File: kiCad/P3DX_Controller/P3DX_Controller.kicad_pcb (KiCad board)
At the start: 2 copper layers, 125 x 80 mm, 25 parts, among them J1 Conn_01x10_Pin, J2 Conn_01x26_Pin, J3 Conn_01x10_Pin, J4 Conn_01x16_Pin, J5 Conn_01x03_Pin, J6 Conn_01x05_Pin, U1 TXS0108EPW, U3 ESP32-DevKitC

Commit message: 20251201
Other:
- board text added: "Pioneer 3DX Mobile Robot Controller Department: ATIx/Mechatronics Design by: Gerard Harkema © 2025 https://avansmechatronica.github.io/pioneer3dx_ROS2/"
- board text removed: "Pioneer 3DX Mobile Robot Controller Department: ATIx/Mechatronics Design by: Gerard Harkema © 2025"
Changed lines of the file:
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@@
 		)
 	)
-	(gr_text "Pioneer 3DX Mobile Robot Controller\nDepartment: ATIx/Mechatronics\nDesign by: Gerard Harkema © 2025\n"
+	(gr_text "Pioneer 3DX Mobile Robot Controller\nDepartment: ATIx/Mechatronics\nDesign by: Gerard Harkema © 2025\nhttps://avansmechatronica.github.io/pioneer3dx_ROS2/"
 		(locked yes)
 		(at 111.95 125.6 0)

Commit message: 20251202
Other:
- board text added: "User Control Panel"
- board text removed: "User Panel Control"
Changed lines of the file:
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@@
 			(outputformat 1)
 			(mirror no)
-			(drillshape 1)
+			(drillshape 0)
 			(scaleselection 1)
-			(outputdirectory "")
+			(outputdirectory "Gerber/")
 		)
 	)
@@
 		)
 	)
-	(gr_text "User Panel Control"
+	(gr_text "User Control Panel"
 		(at 51.9225 88.9233 90)
 		(layer "F.SilkS")
@@
 				)
 			)
+		)
+	)
+	(dimension
+		(type orthogonal)
+		(layer "User.2")
+		(pts
+			(xy 175 130) (xy 175 50)
+		)
+		(height 23.5)
+		(orientation 1)
+		(format
+			(prefix "")
+			(suffix "")
+			(units 2)
+			(units_format 0)
+			(precision 1)
+		)
+		(style
+			(thickness 0.1)
+			(arrow_length 1.27)
+			(text_position_mode 0)
+			(arrow_direction outward)
+			(extension_height 0.58642)
+			(extension_offset 0.5)
+			(keep_text_aligned yes)
+		)
+		(gr_text "80,0"
+			(at 197.35 90 90)
+			(layer "User.2")
+			(effects
+				(font
+					(size 1 1)
+					(thickness 0.15)
+				)
+			)
+		)
+	)
+	(dimension
+		(type orthogonal)
+		(layer "User.2")
+		(pts
+			(xy 50 130) (xy 175 130)
+		)
+		(height 10.5)
+		(orientation 0)
+		(format
+			(prefix "")
+			(suffix "")
+			(units 2)
+			(units_format 1)
+			(precision 4)
+		)
+		(style
+			(thickness 0.1)
+			(arrow_length 1.27)
+			(text_position_mode 0)
+			(arrow_direction outward)
+			(extension_height 0.58642)
+			(extension_offset 0.5)
+			(keep_text_aligned yes)
+		)
+		(gr_text "125,0000 mm"
+			(at 112.5 139.35 0)
+			(layer "User.2")
+			(effects
+				(font
+					(size 1 1)
+					(thickness 0.15)
+				)
+			)

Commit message: 20251202
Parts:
- removed the R5 at (146.2, 63.5)
- removed U4: ~, p3dx:MPU6050
- added J6: Conn_01x03_Pin, Connector_PinHeader_2.54mm:PinHeader_1x03_P2.54mm_Vertical, F.Cu at (129.1, 70.9)
- added R4: DO NOT PLACE, Resistor_THT:R_Axial_DIN0204_L3.6mm_D1.6mm_P7.62mm_Horizontal, F.Cu at (64.7, 71.8)
- moved R5 10.7 mm to (64.7, 77.9), turned to -90 degrees
- moved U1 9.10 mm to (87.4, 82.4)
- moved CP1 4.10 mm to (119.3, 79.1)
- moved CP2 4.10 mm to (119.3, 69.8)
- moved C1 4.10 mm to (116.8, 74.5)
- moved C2 4.10 mm to (116.8, 83.8)
- renumbered C3 to C1, C4 to C2, G*** to G1, HOLE4 to HOLE3, HOLE3 to HOLE4, J6 to J7, R4 to R1, R1 to R2, R2 to R5, U3 to U2, U2 to U3
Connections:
- J1 pad 1: /front_bumper -> /bumper
- J1 pad 2: /front_bumper -> /bumper
- J1 pad 3: /front_bumper -> /bumper
- J1 pad 4: /front_bumper -> /bumper
- J1 pad 5: /front_bumper -> /bumper
- J1 pad 6: /front_bumper -> /bumper
- J1 pad 7: /front_bumper -> /bumper
- J1 pad 8: /front_bumper -> /bumper
- J3 pad 1: /rear_bumper -> /bumper
- J3 pad 2: /rear_bumper -> /bumper
- J3 pad 3: /rear_bumper -> /bumper
- J3 pad 4: /rear_bumper -> /bumper
- J3 pad 5: /rear_bumper -> /bumper
- J3 pad 6: /rear_bumper -> /bumper
- J3 pad 7: /rear_bumper -> /bumper
- J3 pad 8: /rear_bumper -> /bumper
- R1 pad 2: /front_bumper -> /bumper
- U2 pad 12: /imu_int -> /lidar-motor
- U2 pad 16: /R_ENCODER_A_LV -> unconnected-(U3-SD_DATA2/GPIO9-Pad16)
- U2 pad 17: /L_ENCODER_A_LV -> unconnected-(U3-SD_DATA3/GPIO10-Pad17)
- U2 pad 20: /R_MOTOR_DIR -> unconnected-(U3-SD_CLK/GPIO6-Pad20)
- U2 pad 21: /L_ENCODER_B_LV -> unconnected-(U3-SD_DATA0/GPIO7-Pad21)
- U2 pad 22: /R_ENCODER_B_LV -> unconnected-(U3-SD_DATA1/GPIO8-Pad22)
- U2 pad 24: unconnected-(U3-ADC2_CH2/GPIO2-Pad24) -> /R_ENCODER_B_LV
- U2 pad 25: unconnected-(U3-GPIO0/BOOT/ADC2_CH1-Pad25) -> /L_ENCODER_B_LV
- U2 pad 33: /i2c-sda -> /R_ENCODER_A_LV
- U2 pad 36: /i2c-scl -> /L_ENCODER_A_LV
- U2 pad 7: /front_bumper -> /R_MOTOR_DIR
- U2 pad 8: /rear_bumper -> /bumper
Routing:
- net /bumper: track 0.00 -> 150.0 mm
- net /rear_bumper: track 123.5 -> 0.00 mm, vias 1 -> 0
- net /lidar-motor: track 0.00 -> 80.1 mm
- net /front_bumper: track 55.5 -> 0.00 mm
- net +3V3: track 170.2 -> 117.1 mm, vias 1 -> 0
- net /R_MOTOR_DIR: track 129.7 -> 77.8 mm
- net /i2c-scl: track 47.2 -> 0.00 mm, vias 1 -> 0
- net /i2c-sda: track 41.5 -> 0.00 mm
- net /imu_int: track 22.7 -> 0.00 mm, vias 1 -> 0
- net /ucp_status_lv: track 95.4 -> 75.3 mm, vias 2 -> 1
- net /L_ENCODER_B_LV: track 81.0 -> 61.5 mm
- net /ucp_motors_lv: track 28.8 -> 13.2 mm, vias 1 -> 0
- net /L_ENCODER_B: track 20.0 -> 35.4 mm, vias 0 -> 1
- net /R_ENCODER_B_LV: track 77.2 -> 62.4 mm
- net /ucp_motors: track 72.0 -> 58.5 mm
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
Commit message: 20251203
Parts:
- added R6: DO NOT PLACE, Resistor_THT:R_Axial_DIN0204_L3.6mm_D1.6mm_P7.62mm_Horizontal, F.Cu at (137.0, 137.1)
- U2: value ESP32-DevKitC -> ESP32-S3-DevKitC; footprint PCM_Espressif:ESP32-DevKitC -> PCM_Espressif:ESP32-S3-DevKitC
- moved U2 14.6 mm to (112.9, 94.1)
- turned U3 to 180 degrees
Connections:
- U2 pad 10: /L_MOTOR_DIR -> unconnected-(U2-GPIO17/ADC2_CH6-Pad10)
- U2 pad 11: /R_MOTOR_PWM -> unconnected-(U2-GPIO18/ADC2_CH7-Pad11)
- U2 pad 12: /lidar-motor -> unconnected-(U2-GPIO8/ADC1_CH7-Pad12)
- U2 pad 13: /display_RS_DC -> unconnected-(U2-GPIO3/ADC1_CH2-Pad13)
- U2 pad 14: GND -> unconnected-(U2-GPIO46-Pad14)
- U2 pad 15: /display_rst -> unconnected-(U2-GPIO9/ADC1_CH8-Pad15)
- U2 pad 19: VCC -> unconnected-(U2-GPIO13/ADC2_CH2-Pad19)
- U2 pad 2: unconnected-(U3-CHIP_PU-Pad2) -> +3V3
- U2 pad 21: unconnected-(U3-SD_DATA0/GPIO7-Pad21) -> VCC
- U2 pad 22: unconnected-(U3-SD_DATA1/GPIO8-Pad22) -> GND
- U2 pad 23: /ucp_status_lv -> GND
- U2 pad 24: /R_ENCODER_B_LV -> GND
- U2 pad 25: /L_ENCODER_B_LV -> unconnected-(U2-GPIO19/USB_D--Pad25)
- U2 pad 26: /MOTOR_ENABLE -> unconnected-(U2-GPIO20/USB_D+-Pad26)
- U2 pad 27: /lidar-tx -> unconnected-(U2-GPIO21-Pad27)
- U2 pad 28: /lidar-rx -> unconnected-(U2-GPIO47-Pad28)
- U2 pad 29: /display_cs -> unconnected-(U2-GPIO48-Pad29)
- U2 pad 3: /ucp_motors_lv -> unconnected-(U2-CHIP_PU-Pad3)
- U2 pad 30: /display_clk -> unconnected-(U2-GPIO45-Pad30)
- U2 pad 31: /display_not_used -> unconnected-(U2-GPIO0-Pad31)
- U2 pad 32: GND -> unconnected-(U2-GPIO35-Pad32)
- U2 pad 33: /R_ENCODER_A_LV -> unconnected-(U2-GPIO36-Pad33)
- U2 pad 36: /L_ENCODER_A_LV -> unconnected-(U2-GPIO39/MTCK-Pad36)
- U2 pad 37: /display_sda -> unconnected-(U2-GPIO40/MTDO-Pad37)
- U2 pad 38: GND -> unconnected-(U2-GPIO41/MTDI-Pad38)
- U2 pad 4: /ucp_buzzer_pwm_lv -> unconnected-(U2-GPIO4/ADC1_CH3-Pad4)
- U2 pad 5: /V_BATTERY_MEASUREMENT -> unconnected-(U2-GPIO5/ADC1_CH4-Pad5)
- U2 pad 6: /ucp_reset_lv -> unconnected-(U2-GPIO6/ADC1_CH5-Pad6)
- U2 pad 7: /R_MOTOR_DIR -> unconnected-(U2-GPIO7/ADC1_CH6-Pad7)
- U2 pad 8: /bumper -> unconnected-(U2-GPIO15/ADC2_CH4/32K_P-Pad8)
- U2 pad 9: /L_MOTOR_PWM -> unconnected-(U2-GPIO16/ADC2_CH5/32K_N-Pad9)
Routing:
- net /bumper: track 150.0 -> 0.00 mm
- net VCC: track 149.6 -> 0.00 mm
- net +3V3: track 117.1 -> 0.00 mm
- net /lidar-tx: track 115.4 -> 0.00 mm, vias 1 -> 0
- net /MOTOR_ENABLE: track 113.7 -> 0.00 mm, vias 1 -> 0
- net /lidar-rx: track 111.5 -> 0.00 mm, vias 1 -> 0
- net /L_MOTOR_PWM: track 86.1 -> 0.00 mm, vias 2 -> 0
- net /L_MOTOR_DIR: track 85.7 -> 0.00 mm, vias 1 -> 0
- net /R_MOTOR_PWM: track 82.4 -> 0.00 mm, vias 1 -> 0
- net /lidar-motor: track 80.1 -> 0.00 mm
- net /R_MOTOR_DIR: track 77.8 -> 0.00 mm, vias 1 -> 0
- net /ucp_status_lv: track 75.3 -> 0.00 mm, vias 1 -> 0
- net /R_ENCODER_B_LV: track 62.4 -> 0.00 mm, vias 1 -> 0
- net /L_ENCODER_B_LV: track 61.5 -> 0.00 mm, vias 1 -> 0
- net /ucp_motors: track 58.5 -> 0.00 mm, vias 1 -> 0
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
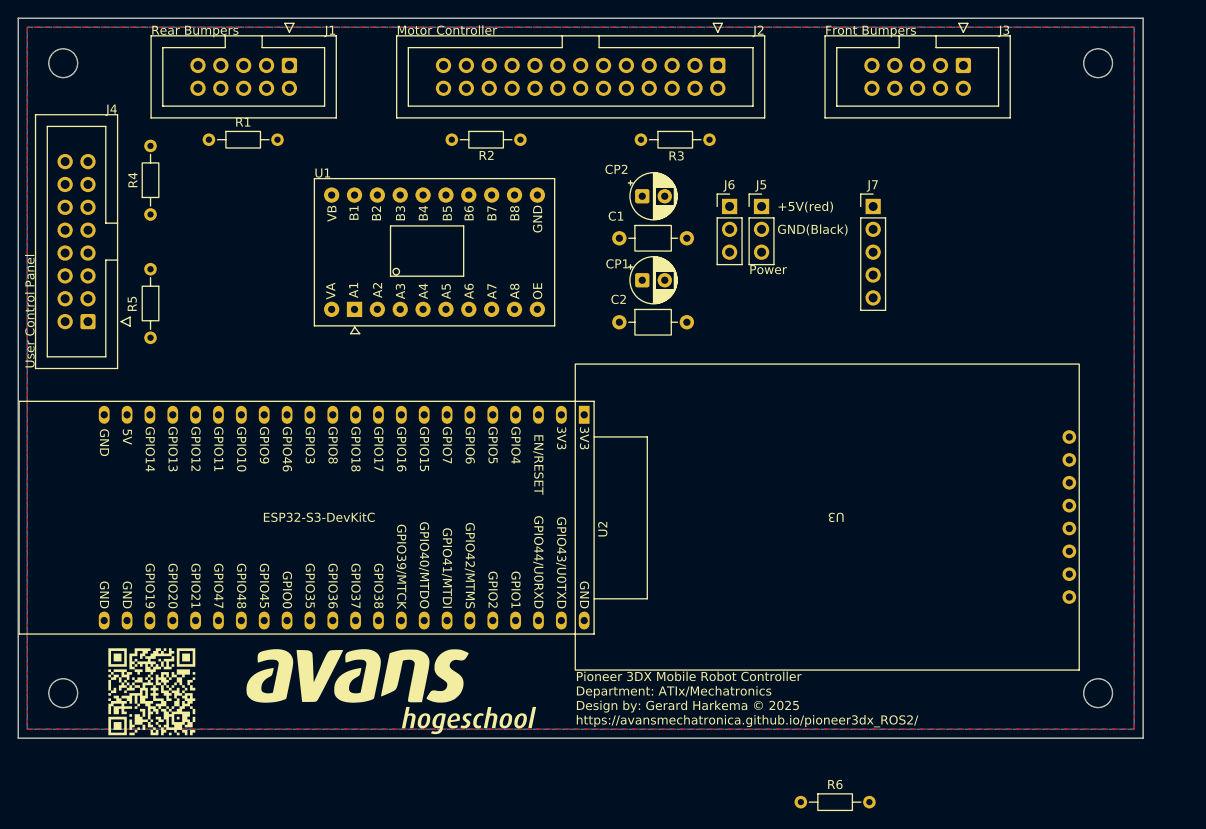
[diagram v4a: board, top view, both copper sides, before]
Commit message: esp32-s3 change
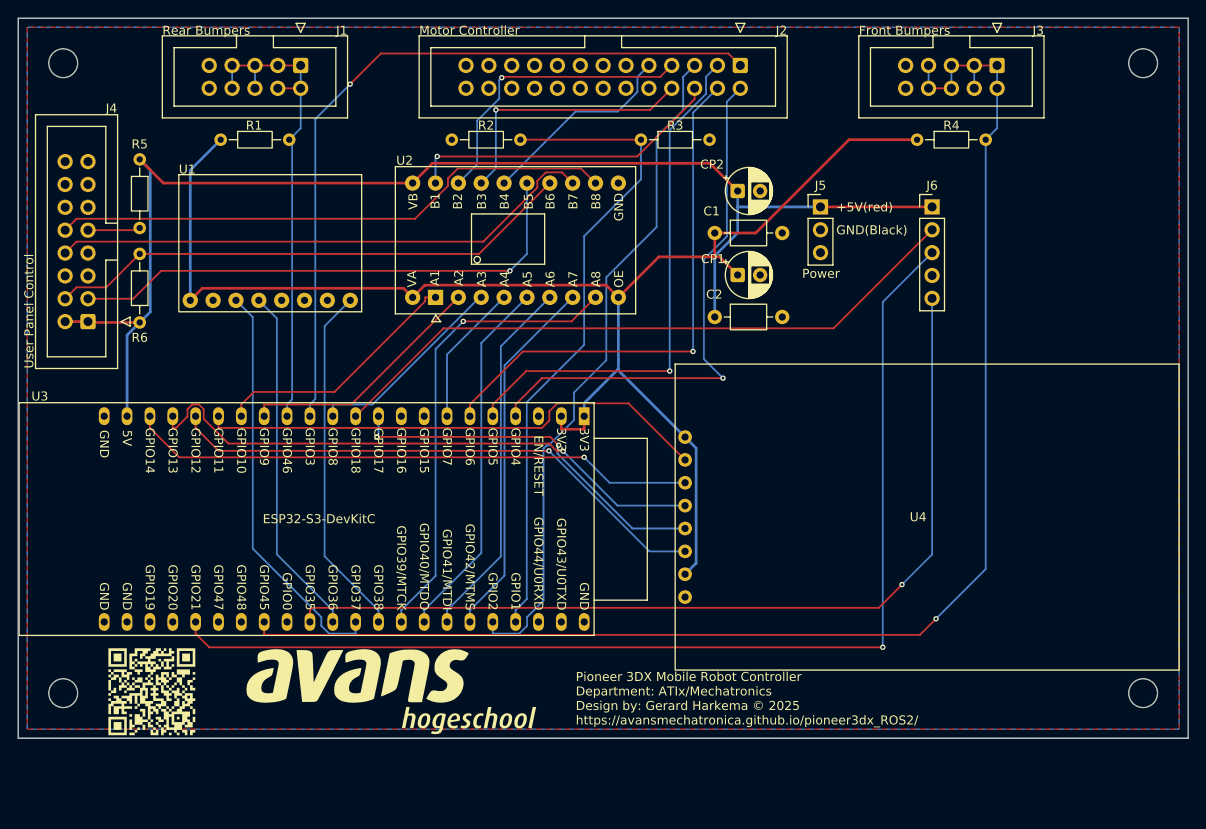
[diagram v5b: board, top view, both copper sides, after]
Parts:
- removed the J6 at (129.1, 70.9)
- removed the R6 at (137.0, 137.1)
- removed the U2 at (112.9, 94.1)
- added R5: DO NOT PLACE, Resistor_THT:R_Axial_DIN0204_L3.6mm_D1.6mm_P7.62mm_Horizontal, F.Cu at (63.5, 65.7)
- added U1: ~, p3dx:MPU6050, F.Cu at (64.0, 76.3)
- added U3: ESP32-S3-DevKitC, PCM_Espressif:ESP32-S3-DevKitC, F.Cu at (112.9, 94.2)
- moved R4 85.6 mm to (149.9, 63.5), turned to 0 degrees
- moved U4 11.1 mm to (151.0, 105.4), turned to 0 degrees
- moved C1 10.6 mm to (127.4, 73.9)
- moved C2 10.6 mm to (127.4, 83.2)
- moved CP1 10.6 mm to (129.9, 78.5)
- moved CP2 10.6 mm to (129.9, 69.2)
- moved U2 9.10 mm to (96.4, 81.0)
- moved J5 6.55 mm to (139.2, 71.0)
- moved J6 6.55 mm to (151.6, 71.0)
- moved R6 6.04 mm to (63.5, 83.8), turned to 90 degrees
- moved HOLE2 5.00 mm to (175.0, 55.0)
- moved HOLE4 5.00 mm to (175.0, 125.0)
- moved J3 3.75 mm to (158.8, 55.2)
- moved J2 2.50 mm to (130.2, 55.2)
- moved R1 1.31 mm to (72.5, 63.5)
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- renumbered G*** to G2, J7 to J6, R5 to R6, U1 to U2, U3 to U4
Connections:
- J1 pad 1: /bumper -> /front_bumper
- J1 pad 2: /bumper -> /front_bumper
- J1 pad 3: /bumper -> /front_bumper
- J1 pad 4: /bumper -> /front_bumper
- J1 pad 5: /bumper -> /front_bumper
- J1 pad 6: /bumper -> /front_bumper
- J1 pad 7: /bumper -> /front_bumper
- J1 pad 8: /bumper -> /front_bumper
- J3 pad 1: /bumper -> /rear_bumper
- J3 pad 2: /bumper -> /rear_bumper
- J3 pad 3: /bumper -> /rear_bumper
- J3 pad 4: /bumper -> /rear_bumper
- J3 pad 5: /bumper -> /rear_bumper
- J3 pad 6: /bumper -> /rear_bumper
- J3 pad 7: /bumper -> /rear_bumper
- J3 pad 8: /bumper -> /rear_bumper
- R1 pad 2: /bumper -> /front_bumper
- R4 pad 1: VCC -> +3V3
- R4 pad 2: /ucp_power_led -> /rear_bumper
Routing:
- net +3V3: track 0.00 -> 161.4 mm
- net /rear_bumper: track 0.00 -> 156.3 mm, vias 0 -> 1
- net VCC: track 0.00 -> 144.8 mm
- net /lidar-rx: track 0.00 -> 124.4 mm, vias 0 -> 1
- net /lidar-motor: track 0.00 -> 101.5 mm, vias 0 -> 1
- net /L_MOTOR_PWM: track 0.00 -> 84.1 mm, vias 0 -> 1
- net /MOTOR_ENABLE: track 0.00 -> 75.6 mm
- net /V_BATTERY_MEASUREMENT: track 0.00 -> 72.7 mm
- net /lidar-tx: track 0.00 -> 72.6 mm
- net /display_rst: track 0.00 -> 65.1 mm, vias 0 -> 1
- net /display_RS_DC: track 0.00 -> 63.3 mm, vias 0 -> 1
- net /ucp_status: track 0.00 -> 62.9 mm
- net /display_clk: track 0.00 -> 61.4 mm, vias 0 -> 1
- net /ucp_buzzer_pwm: track 0.00 -> 61.0 mm
- net /L_MOTOR_DIR: track 0.00 -> 60.3 mm, vias 0 -> 1
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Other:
- board size 125 x 80 mm -> 130 x 80 mm
- board text added: "User Panel Control"
- board text removed: "User Control Panel"

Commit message: 20251204
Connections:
- J2 pad 10: unconnected-(J2-Pin_10-Pad10) -> /R_ENCODER_B
- J2 pad 12: unconnected-(J2-Pin_12-Pad12) -> /L_ENCODER_B
- J2 pad 22: GND -> /V_BATTERY
- J2 pad 7: /R_ENCODER_A -> unconnected-(J2-Pin_7-Pad7)
- J2 pad 8: /R_ENCODER_B -> /R_ENCODER_A
- J2 pad 9: /L_ENCODER_B -> unconnected-(J2-Pin_9-Pad9)
- J4 pad 11: unconnected-(J4-Pin_11-Pad11) -> /V_BATTERY
- J4 pad 12: GND -> unconnected-(J4-Pin_12-Pad12)
- R2 pad 1: GND -> /V_BATTERY
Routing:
- net /V_BATTERY: track 0.00 -> 53.9 mm
- net /R_MOTOR_DIR: track 58.9 -> 87.5 mm
- net /display_clk: track 61.4 -> 80.7 mm, vias 1 -> 2
- net VCC: track 144.8 -> 155.8 mm, vias 0 -> 1
- net /display_cs: track 57.5 -> 68.2 mm, vias 0 -> 3
- net /lidar-tx: track 72.6 -> 83.0 mm, vias 0 -> 1
- net /display_rst: track 65.1 -> 74.0 mm, vias 1 -> 2
- net /display_sda: track 41.6 -> 50.2 mm, vias 2 -> 1
- net /display_RS_DC: track 63.3 -> 71.4 mm, vias 1 -> 0
- net +3V3: track 161.4 -> 167.5 mm, vias 0 -> 1
- net /L_MOTOR_DIR: track 60.3 -> 55.2 mm
- net /R_ENCODER_A: track 33.2 -> 28.1 mm, vias 1 -> 0
- net /L_ENCODER_A_LV: track 28.1 -> 33.0 mm, vias 0 -> 1
- net /R_ENCODER_A_LV: track 27.8 -> 32.6 mm, vias 0 -> 1
- net /L_ENCODER_B: track 22.5 -> 17.9 mm
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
